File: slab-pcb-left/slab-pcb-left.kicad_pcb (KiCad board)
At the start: 2 copper layers, 158 x 104 mm, 129 parts, among them J1 MagnetR, J2 MagnetL, J3 TRRS_R, J4 TRRS_L, J5 SSD1306, J6 Conn_01x06, Q1 MMBT3906, SW1 RotaryEncoder, U1 Seeeduino Xiao rp2040, U2 PCA9555PW, U3 PCA9555PW, U4 ADS1110, U5 SN74AHCT125PWR

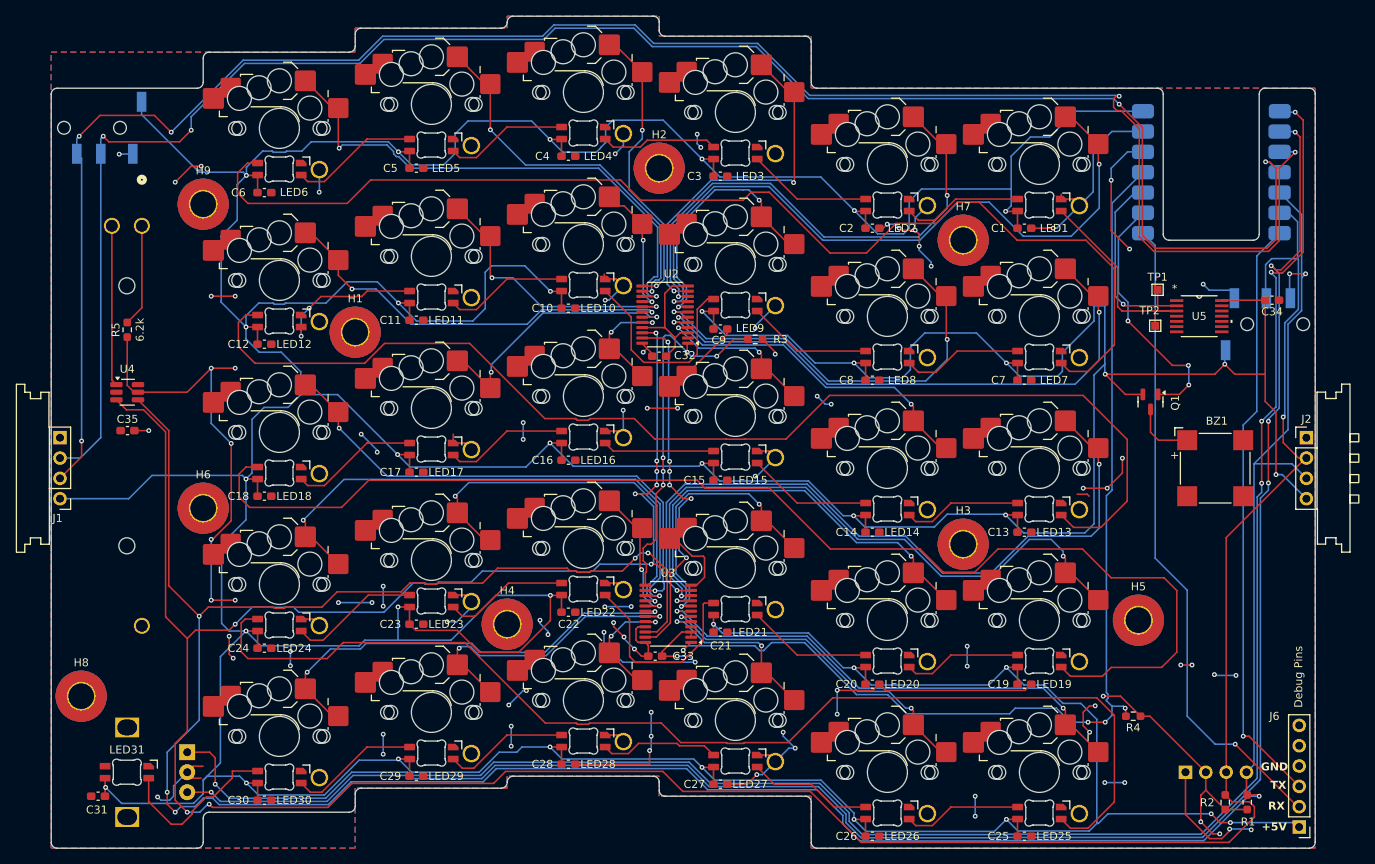
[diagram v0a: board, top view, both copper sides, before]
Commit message: feat: use slots instead of overlapped drill hits
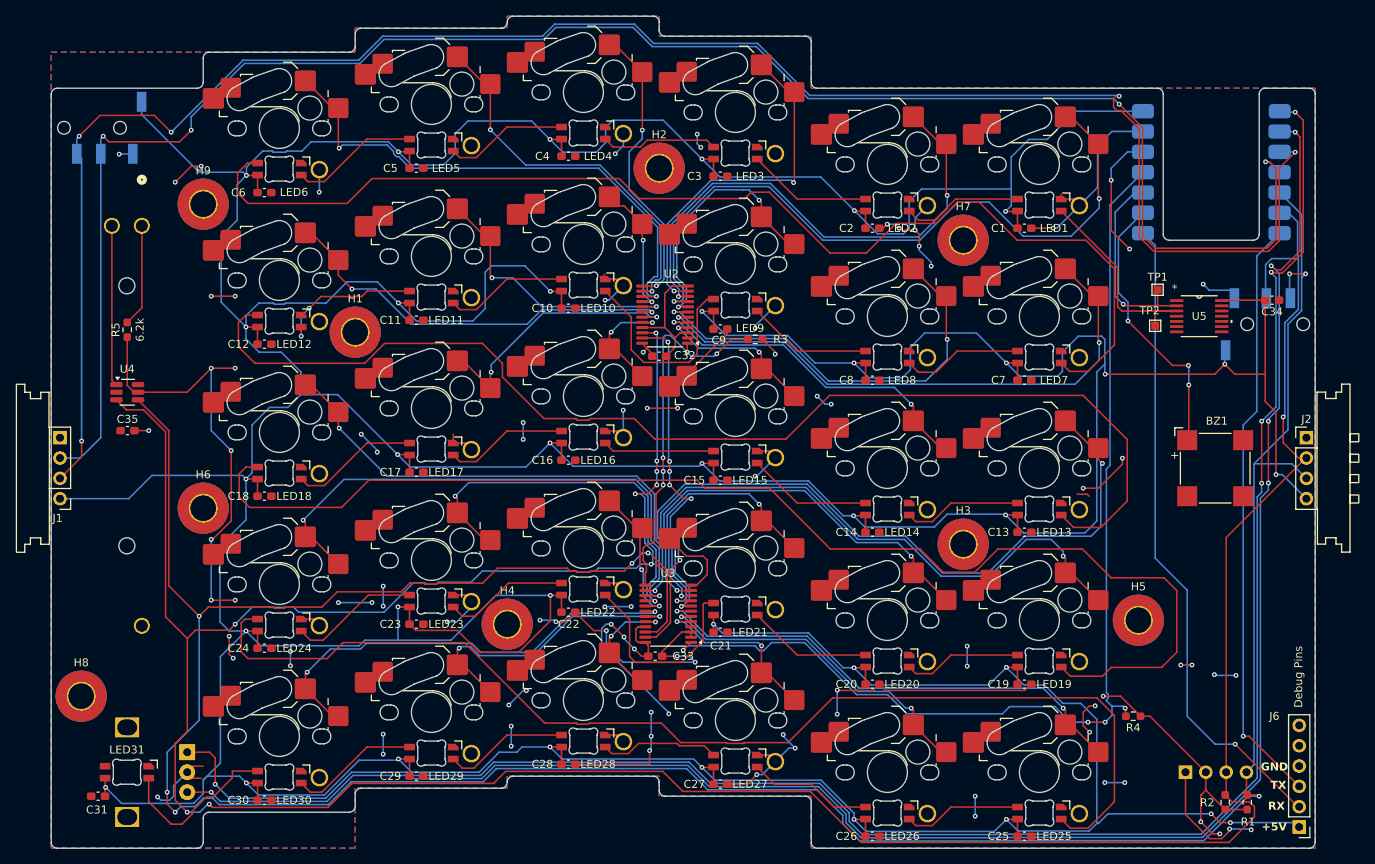
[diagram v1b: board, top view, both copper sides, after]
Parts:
- removed Q1: MMBT3906, Package_TO_SOT_SMD:SOT-23
- BZ1: footprint Buzzer_Beeper:MagneticBuzzer_CUI_CMT-8504-100-SMT -> CustomFootprints:buzzer
- U5: value SN74AHCT125PWR -> (none)
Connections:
- BZ1 pad 1: Net-(BZ1-+) -> /BUZZER
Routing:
- net +3V3: track 150.5 -> 165.3 mm
- net VBUS: track 1009.5 -> 996.7 mm
- net Net-(BZ1-+): track 7.86 -> 0.00 mm
- net GND: track 279.6 -> 287.3 mm
- net /BUZZER: track 31.9 -> 34.6 mm
- net /KEY13: track 90.7 -> 91.9 mm
- net Net-(LED12-DOUT): track 146.4 -> 147.4 mm
- net /KEY19: track 78.8 -> 79.8 mm
- net /KEY21: track 34.0 -> 34.9 mm
- net /KEY20: track 56.8 -> 57.7 mm
- net /KEY18: track 65.4 -> 64.7 mm

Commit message: feat: bump to 3.2
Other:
- board text added: "version 3.2 'nowhere'"
- board text removed: "version 3.1 'nowhere'"
